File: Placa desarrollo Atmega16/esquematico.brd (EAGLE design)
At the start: 82.7 x 90.2 mm, 34 parts, among them IC1 MEGA16-P, IC2 7805DT, IC3 7805DT, Q2 16MHz, X1 PN61729-S

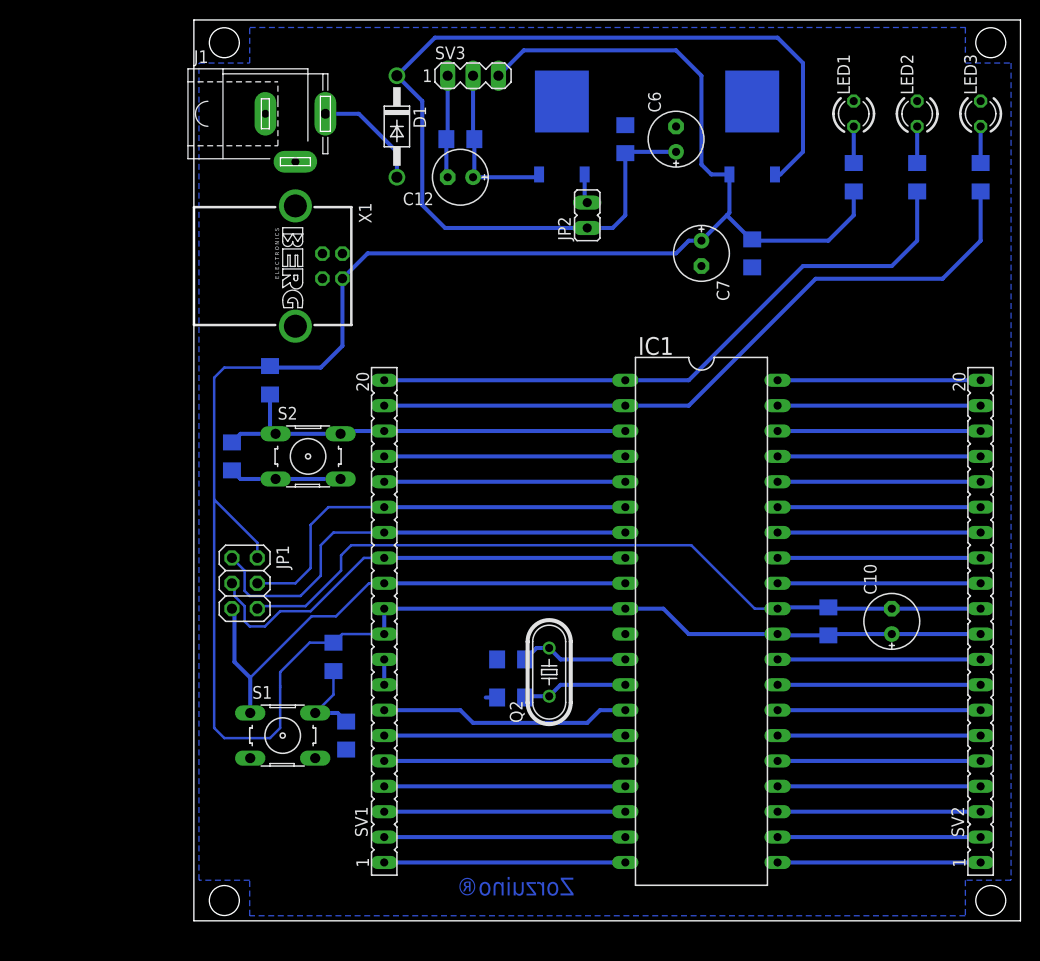
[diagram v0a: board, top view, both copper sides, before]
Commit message: Modifique el jumper del lm7833
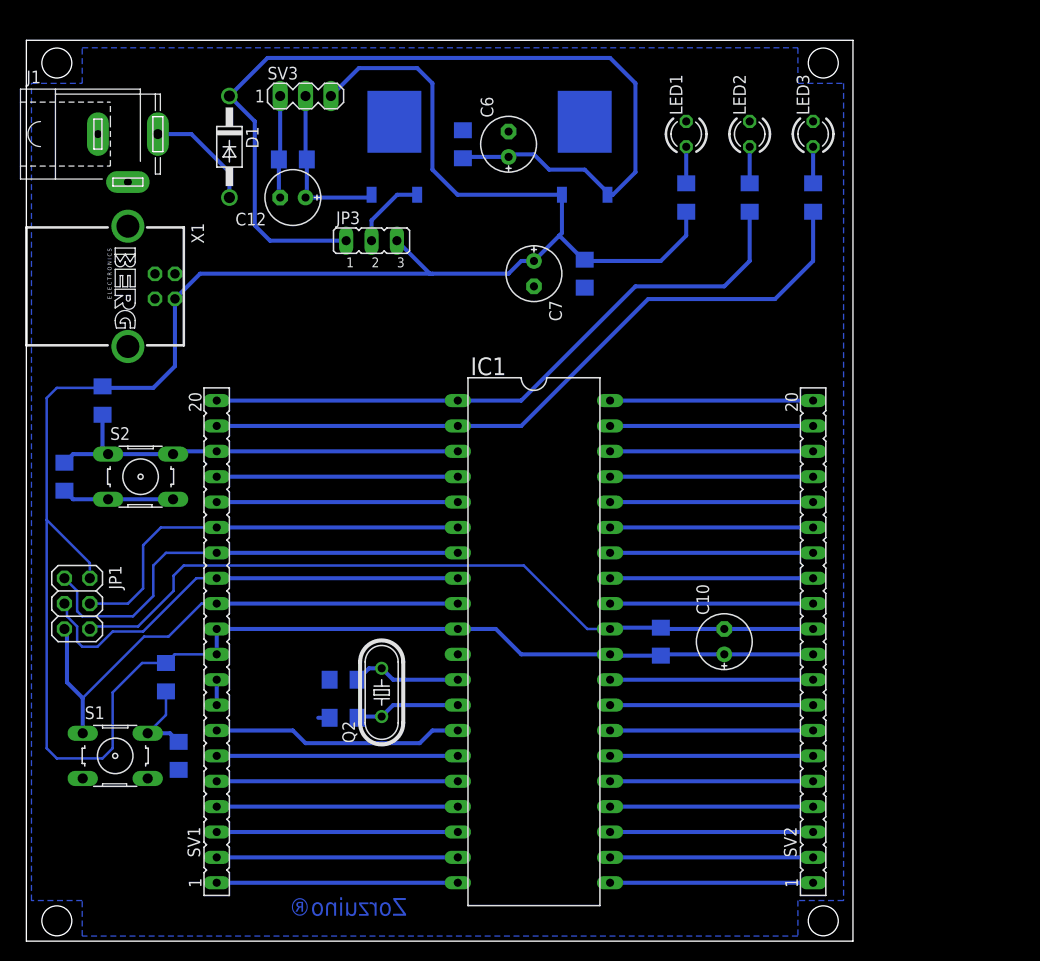
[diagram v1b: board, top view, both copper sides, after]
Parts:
- removed JP2: (no value), jumper:JP1
- added JP3: (no value), jumper:JP2
- moved C9 16.9 mm to (64.0, 27.9)
- moved LED2 16.9 mm to (72.9, 78.7)
- moved R3 16.9 mm to (72.9, 72.4)
- moved C1 16.9 mm to (15.7, 16.5)
- moved C5 16.9 mm to (56.4, 64.8)
- moved C7 16.9 mm to (51.3, 64.8)
- moved C8 16.9 mm to (4.32, 44.5)
- moved IC1 16.9 mm to (51.3, 27.9)
- moved IC3 16.9 mm to (56.4, 77.5)
- moved Q2 16.9 mm to (36.1, 22.9)
- moved R1 16.9 mm to (14.5, 24.4)
- moved S2 16.9 mm to (11.9, 44.5)
- moved SV1 16.9 mm to (19.6, 27.9)
- moved SV3 16.9 mm to (28.4, 82.5)
- moved C11 16.9 mm to (27.2, 76.2)
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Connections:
- net N$5: now also JP3.2; no longer JP2.2
- net VCC_5V: now also JP3.3
- net VIN: now also JP3.1; no longer JP2.1
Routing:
- net VIN: track 103.0 -> 96.1 mm
- net N$5: track 2.93 -> 7.66 mm
- net VCC_5V: track 249.1 -> 253.9 mm

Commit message: Modifique el ancho de las pistas. Hay algunos problemas con la interconexion de masas
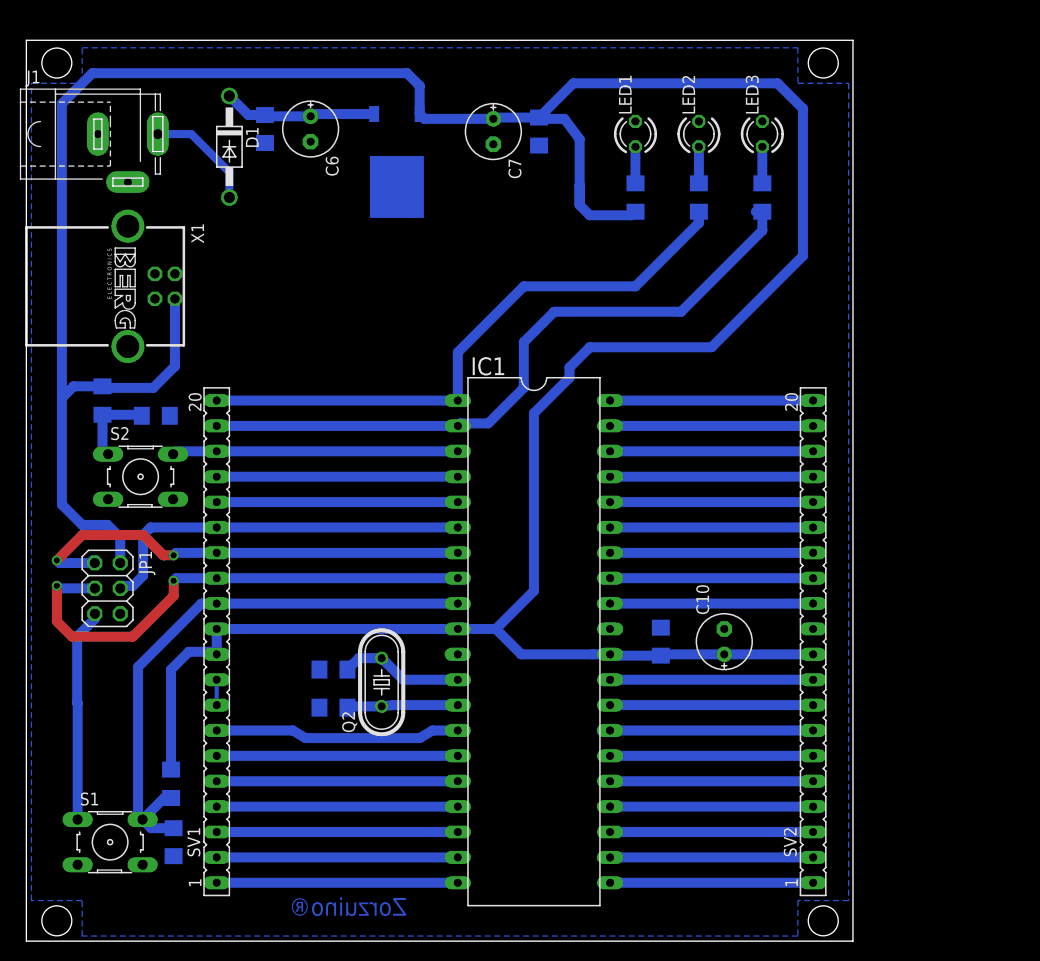
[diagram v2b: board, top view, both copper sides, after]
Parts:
- removed C11: 100nF, rcl:C1206
- removed C12: 10uF, rcl:E2,5-6E
- removed IC2: 7805DT, linear:TO252
- removed JP3: (no value), jumper:JP2
- removed SV3: (no value), con-lstb:MA03-1
- moved C6 19.9 mm to (29.0, 79.2), turned to 270 degrees
- moved C4 19.9 mm to (24.4, 79.2), turned to 270 degrees
- moved IC3 18.9 mm to (37.6, 75.9), turned to 180 degrees
- moved C5 14.9 mm to (51.8, 79.0)
- moved C7 14.8 mm to (47.2, 79.0)
- moved C8 11.0 mm to (13.5, 50.5), turned to 180 degrees
- moved R1 10.7 mm to (15.0, 13.7)
- moved C1 8.65 mm to (15.2, 7.87)
- moved S1 8.65 mm to (8.89, 7.87)
- moved LED1 5.08 mm to (61.5, 78.7)
- moved LED2 5.08 mm to (67.8, 78.7)
- moved LED3 5.08 mm to (74.2, 78.7)
- moved R2 5.08 mm to (61.5, 72.4)
- moved R3 5.08 mm to (67.8, 72.4)
- moved R4 5.08 mm to (74.2, 72.4)
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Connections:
- removed net N$5: IC2.1, JP3.2
- removed net VCC_3V: C11.1, C12.+, IC2.2, SV3.2
- net GND: no longer C11.2, C12.-, IC2.3, SV3.1
- net VCC_5V: no longer JP3.3, SV3.3
- net VIN: no longer JP3.1
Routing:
- net GND: track 104.1 -> 2.91 mm
- net VIN: track 96.1 -> 15.4 mm
- net VCC_5V: track 253.9 -> 322.3 mm
- net RESET: track 61.1 -> 78.6 mm
- net VCC_3V: track 17.0 -> 0.00 mm
- net N$5: track 7.66 -> 0.00 mm
- net PB2: track 43.8 -> 37.1 mm
- net SCK: track 46.5 -> 52.6 mm, vias 0 -> 2
- net MOSI: track 42.5 -> 38.7 mm
- net PB1: track 71.5 -> 67.9 mm
- net PB0: track 64.1 -> 60.7 mm
- net XTAL2: track 11.0 -> 12.4 mm
- net PD0: track 25.2 -> 24.6 mm
- net XTAL1: track 10.6 -> 11.1 mm
- net MISO: track 46.6 -> 46.4 mm, vias 0 -> 2

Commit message: Supuestamente corregi el tema de las masas
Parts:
- moved S2 23.0 mm to (28.7, 60.2)
- moved C8 19.0 mm to (24.1, 66.3), turned to 90 degrees
- moved R5 15.9 mm to (20.3, 62.2), turned to 0 degrees
- moved C3 6.68 mm to (24.6, 26.2)
- moved C2 5.30 mm to (26.2, 22.9)
- moved SV2 3.56 mm to (75.7, 27.9)
- moved C10 3.56 mm to (66.8, 27.9)
- moved C9 3.56 mm to (60.5, 27.9)
- moved IC1 3.56 mm to (47.8, 27.9)
- moved Q2 3.56 mm to (32.5, 23.9)
- moved J1 1.02 mm to (10.7, 77.7)
- moved SV1 0.51 mm to (19.1, 27.9)
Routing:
- net PB2: track 37.1 -> 67.9 mm
- net GND: track 2.91 -> 20.4 mm, vias 0 -> 3
- net VCC_5V: track 322.3 -> 315.9 mm
- net SCK: track 52.6 -> 48.5 mm
- net RESET: track 78.6 -> 75.1 mm
- net MOSI: track 38.7 -> 35.1 mm
- net MISO: track 46.4 -> 42.8 mm
- net PD0: track 24.6 -> 21.1 mm
- net PD6: track 24.1 -> 21.1 mm
- net PD5: track 24.1 -> 21.1 mm
- net PD4: track 24.1 -> 21.1 mm
- net PD3: track 24.1 -> 21.1 mm
- net PD2: track 24.1 -> 21.1 mm
- net PD1: track 24.1 -> 21.1 mm
- net PB4: track 24.1 -> 21.1 mm
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
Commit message: Actualicé el pdf que se necesita para imprimir
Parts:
- moved X1 2.03 mm to (10.7, 61.5)
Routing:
- net GND: track 20.4 -> 23.2 mm
- net VCC_5V: track 315.9 -> 317.8 mm
- net N$6: track 11.4 -> 10.7 mm
